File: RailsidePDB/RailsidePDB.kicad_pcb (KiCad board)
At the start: 2 copper layers, 64 x 94.5 mm, 129 parts, among them SW1 SW_SPST

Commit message: add V3
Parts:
- removed the ? at (53.0, 110.0)
- removed the ? at (65.0, 86.0)
- removed the ? at (55.0, 122.1)
- removed the ? at (89.0, 86.0)
- removed the ? at (57.0, 86.0)
- removed the ? at (61.0, 110.0)
- removed the ? at (109.0, 135.0)
- removed the ? at (97.0, 135.0)
- removed the ? at (105.0, 110.0)
- removed the ? at (87.0, 110.0)
- removed the ? at (103.0, 135.0)
- removed the ? at (59.0, 135.0)
- removed the ? at (55.0, 86.0)
- removed the ? at (59.0, 86.0)
- removed the ? at (113.0, 135.0)
- removed the ? at (69.0, 135.0)
- removed the ? at (55.0, 110.0)
- removed the ? at (101.0, 86.0)
- removed the ? at (65.0, 135.0)
- removed the ? at (91.0, 86.0)
- removed the ? at (87.0, 86.0)
- removed the ? at (105.0, 86.0)
- removed the ? at (95.0, 135.0)
- removed the ? at (69.0, 110.0)
- removed the ? at (85.0, 86.0)
- removed the ? at (93.0, 86.0)
- removed the ? at (67.0, 86.0)
- removed the ? at (97.3, 116.1)
- removed the ? at (109.0, 86.0)
- removed the ? at (57.0, 135.0)
- removed the ? at (57.0, 110.0)
- removed the ? at (91.0, 135.0)
- removed the ? at (113.0, 110.0)
- removed the ? at (73.0, 86.0)
- removed the ? at (75.0, 110.0)
- removed the ? at (79.0, 110.0)
- removed the ? at (71.0, 86.0)
- removed the ? at (101.0, 110.0)
- removed the ? at (97.0, 86.0)
- removed the ? at (55.0, 135.0)
- removed the ? at (99.0, 86.0)
- removed the ? at (111.0, 86.0)
- removed the ? at (69.0, 86.0)
- removed the ? at (71.0, 135.0)
- removed the ? at (91.0, 110.0)
- removed the ? at (55.8, 146.3)
- removed the ? at (93.0, 110.0)
- removed the ? at (75.0, 86.0)
- removed the ? at (89.0, 110.0)
- removed the ? at (73.0, 110.0)
- removed the ? at (97.0, 110.0)
- removed the ? at (95.0, 110.0)
- removed the ? at (103.0, 110.0)
- removed the ? at (101.0, 135.0)
- removed the ? at (107.0, 135.0)
- removed the ? at (98.1, 140.3)
- removed the ? at (63.0, 135.0)
- removed the ? at (107.0, 86.0)
- removed the ? at (111.0, 135.0)
- removed the ? at (56.0, 73.0)
- removed the ? at (77.0, 86.0)
- removed the ? at (63.0, 86.0)
- removed the ? at (103.0, 86.0)
- removed the ? at (99.0, 135.0)
- removed the ? at (85.0, 110.0)
- removed the ? at (107.0, 110.0)
- removed the ? at (87.0, 135.0)
- removed the ? at (83.0, 110.0)
- removed the ? at (67.0, 135.0)
- removed the ? at (59.0, 110.0)
- removed the ? at (105.0, 135.0)
- removed the ? at (93.0, 135.0)
- removed the ? at (98.1, 91.3)
- removed the ? at (83.0, 135.0)
- removed the ? at (95.0, 86.0)
- removed the ? at (83.0, 86.0)
- removed the ? at (73.0, 135.0)
- removed the ? at (65.0, 110.0)
- removed the ? at (71.0, 110.0)
- removed the ? at (61.0, 135.0)
- removed the ? at (109.0, 110.0)
- removed the ? at (55.8, 97.3)
- removed the ? at (81.0, 110.0)
- removed the ? at (99.0, 110.0)
- removed the ? at (53.0, 86.0)
- removed the ? at (81.0, 135.0)
- removed the ? at (79.0, 135.0)
- removed the ? at (67.0, 110.0)
- removed the ? at (89.0, 135.0)
- removed the ? at (111.0, 110.0)
- removed the ? at (53.0, 135.0)
- removed the ? at (77.0, 135.0)
- removed the ? at (113.0, 86.0)
- removed the ? at (61.0, 86.0)
- removed the ? at (75.0, 135.0)
- removed the ? at (81.0, 86.0)
- removed the ? at (63.0, 110.0)
- removed the ? at (85.0, 135.0)
- removed the ? at (79.0, 86.0)
- removed the ? at (77.0, 110.0)
- removed the BT1 at (84.3, 100.3)
- removed the BT1 at (83.5, 125.1)
- removed the BT1 at (84.3, 149.3)
- removed the BT2 at (77.4, 100.2)
- removed the BT2 at (77.4, 149.2)
- removed the BT2 at (76.6, 125.0)
- removed the BT3 at (70.4, 149.1)
- removed the BT3 at (69.6, 124.9)
- removed the BT3 at (70.4, 100.0)
- removed the BT4 at (109.0, 100.4)
- removed the BT4 at (108.2, 125.2)
- removed the BT4 at (109.0, 149.4)
- removed BT5 (x4): Battery, Connector_AMASS:AMASS_XT30UPB-M_1x02_P5.0mm_Vertical
- removed the Fuse at (91.0, 122.4)
- removed the Fuse at (91.9, 97.6)
- removed the Fuse at (91.9, 146.6)
- removed SW1 (x4): SW_SPST, Button_Switch_THT:SW_DIP_SPSTx01_Piano_10.8x4.1mm_W7.62mm_P2.54mm
- added ?: , , F.Cu at (102.2, 66.9)
- added ?: , , F.Cu at (76.3, 79.5)
- moved BT1 4.61 mm to (85.5, 71.5)
- moved BT2 4.54 mm to (78.5, 71.5)
- moved BT3 4.37 mm to (71.5, 71.5)
- moved BT4 0.67 mm to (108.5, 76.0)
- moved ? 0.67 mm to (97.6, 67.0)
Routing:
- net Net-(BT1-+): track 208.9 -> 49.3 mm
- net Net-(BT1--): track 137.2 -> 28.7 mm
- net Net-(SW1-A): track 53.7 -> 13.6 mm
- net Net-(BT4--): track 38.4 -> 8.68 mm
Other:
- board size 64 x 94.5 mm -> 45 x 22.5 mm
- board text added: "Railside Robotics PD 1.3"
- board text removed: "Railside Robotics PD 1.1"

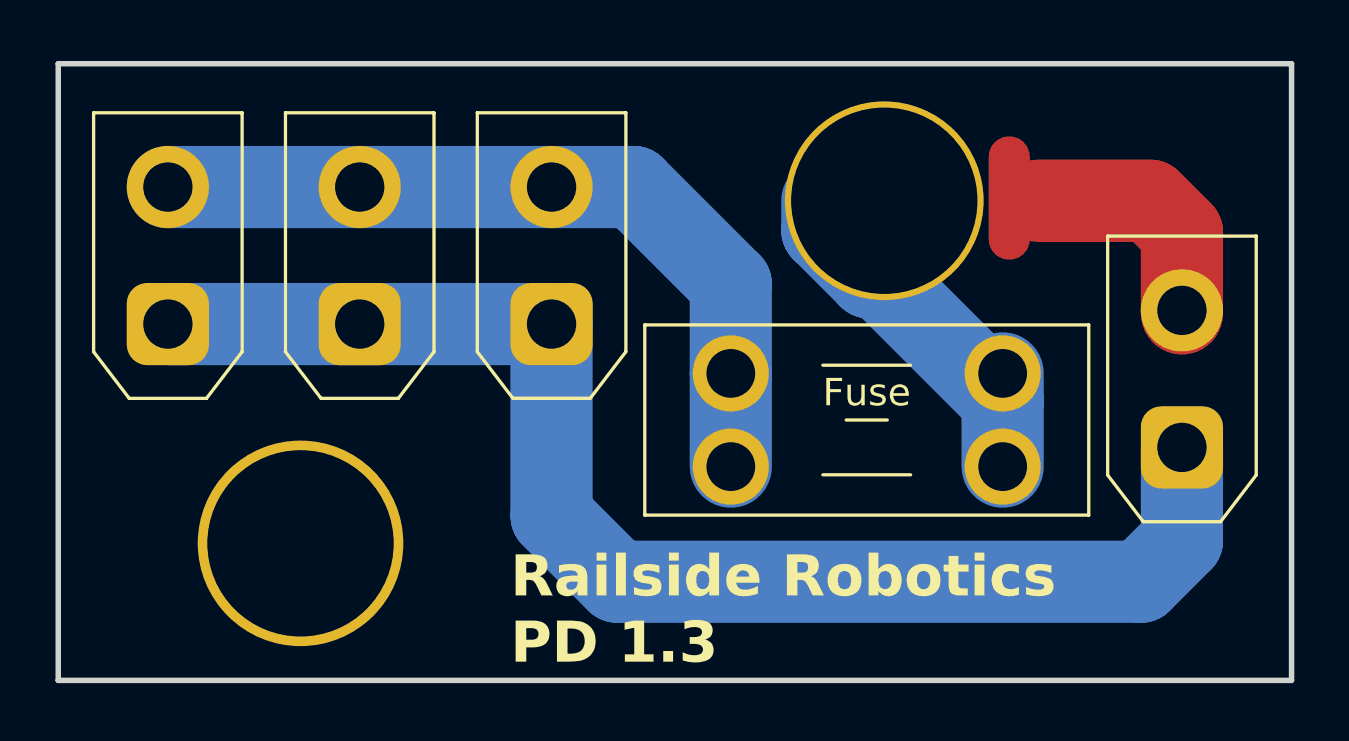
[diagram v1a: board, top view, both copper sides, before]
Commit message: Add cribbage pcb and railside vip area
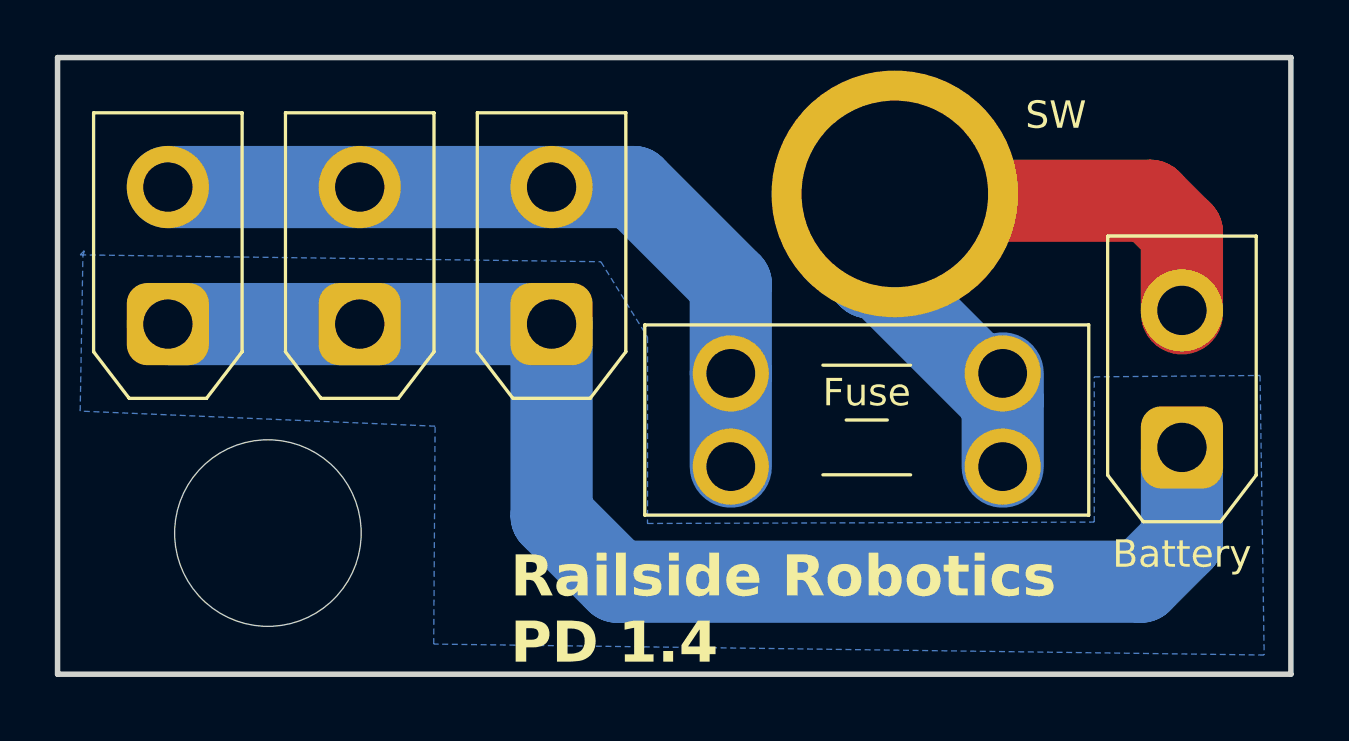
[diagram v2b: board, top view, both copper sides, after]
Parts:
- removed the ? at (97.6, 67.0)
- removed the ? at (102.2, 66.9)
- removed the ? at (76.3, 79.5)
- added ?: , , F.Cu at (121.2, 65.3)
- added ?: , , F.Cu at (98.3, 77.7)
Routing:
- net Net-(BT4--): track 8.68 -> 13.5 mm
- added copper zone on B.Cu, net Net-(BT1--)
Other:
- board text added: "Railside Robotics PD 1.4"
- board text added: "SW"
- board text removed: "Railside Robotics PD 1.3"
